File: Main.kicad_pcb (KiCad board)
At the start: 2 copper layers, 99.1 x 78.7 mm, 41 parts, among them J1 Conn_01x01_Female, J2 Conn_01x01_Female, J3 Conn_01x01_Female, J4 Conn_01x02_Female, J5 Conn_01x01_Female, J6 Conn_01x03, J7 Conn_01x03, Q1 CSD17307Q5A, Q2 CSD17307Q5A, Q3 Si6435ADQ, SW1 SW_Push, SW2 SW_Push, SW3 SW_Push, U1 LTC4002ES8-4.2, U3 LTC6995-1, U4 TPS2557

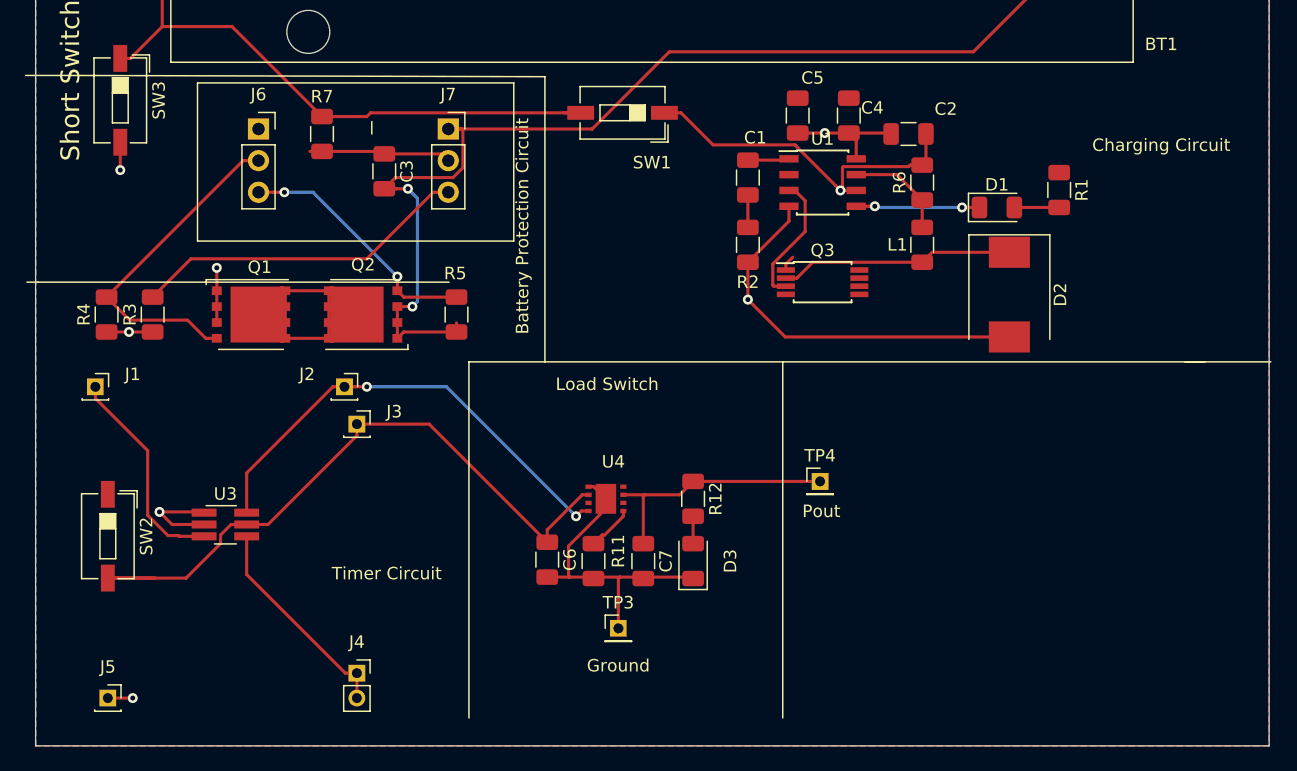
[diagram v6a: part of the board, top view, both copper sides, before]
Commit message: added final silk comments
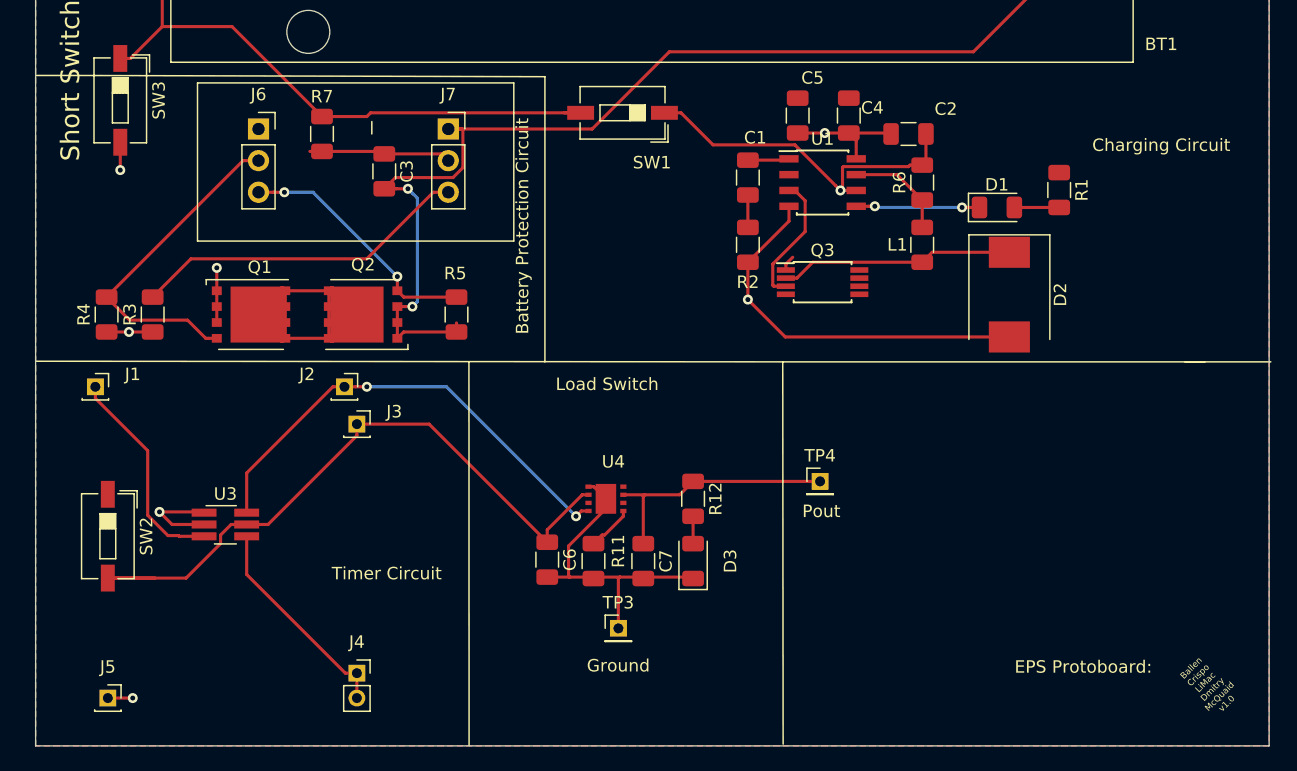
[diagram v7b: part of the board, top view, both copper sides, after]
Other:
- board text added: "Ballen Crispo LiMac Dmitry McQuaid v1.0"
- board text added: "EPS Protoboard:"
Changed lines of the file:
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@@
   (general
     (thickness 1.6)
-    (drawings 29)
+    (drawings 28)
     (tracks 229)
     (zones 0)
@@
     )
   )
+  (gr_text "EPS Protoboard:" (at 134.94 135.9) (layer F.SilkS)
+    (effects (font (size 1 1) (thickness 0.15)))
+  )
+  (gr_text "Ballen\nCrispo\nLiMac\nDmitry\nMcQuaid\nv1.0" (at 145.02 137.41 45) (layer F.SilkS)
+    (effects (font (size 0.5 0.5) (thickness 0.05)))
+  )
   (gr_line (start 50.8 142.24) (end 50.8 63.5) (layer Edge.Cuts) (width 0.05))
   (gr_line (start 149.86 142.24) (end 50.8 142.24) (layer Edge.Cuts) (width 0.05))
@@
     (effects (font (size 1.5 1.5) (thickness 0.3)))
   )
-  (gr_line (start 51 105) (end 50.1 105) (layer F.SilkS) (width 0.12))
-  (gr_line (start 52.6 88.4) (end 50 88.4) (layer F.SilkS) (width 0.12))
   (gr_line (start 143.1 111.4) (end 150 111.4) (layer F.SilkS) (width 0.12))
   (gr_text Pout (at 113.9 123.4) (layer F.SilkS)
@@
   )
   (gr_line (start 110.8 111.4) (end 144.7 111.4) (layer F.SilkS) (width 0.12))
-  (gr_line (start 53.7 88.4) (end 52.6 88.4) (layer F.SilkS) (width 0.12))
+  (gr_line (start 53.7 88.4) (end 50.82 88.4) (layer F.SilkS) (width 0.12))
   (gr_line (start 91.7 88.5) (end 53.7 88.4) (layer F.SilkS) (width 0.12))
   (gr_line (start 91.7 111.4) (end 91.7 88.5) (layer F.SilkS) (width 0.12))
@@
   (gr_line (start 89.2 101.7) (end 63.8 101.7) (layer F.SilkS) (width 0.12))
   (gr_line (start 89.2 89) (end 89.2 101.7) (layer F.SilkS) (width 0.12))
-  (gr_line (start 84 105) (end 51 105) (layer F.SilkS) (width 0.12))
   (gr_line (start 63.8 89) (end 89.2 89) (layer F.SilkS) (width 0.12))
-  (gr_line (start 110.8 111.4) (end 110.8 140) (layer F.SilkS) (width 0.12))
-  (gr_line (start 85.6 111.4) (end 110.8 111.4) (layer F.SilkS) (width 0.12))
+  (gr_line (start 110.8 111.4) (end 110.83 142.1) (layer F.SilkS) (width 0.12))
+  (gr_line (start 50.82 111.35) (end 110.8 111.4) (layer F.SilkS) (width 0.12))
   (gr_text "Charging Circuit" (at 141.2 94) (layer F.SilkS)
     (effects (font (size 1 1) (thickness 0.15)))
@@
   )
   (gr_line (start 77.8 92.1) (end 77.8 93.1) (layer F.SilkS) (width 0.12))
-  (gr_line (start 85.6 111.4) (end 85.6 140) (layer F.SilkS) (width 0.12))
+  (gr_line (start 85.6 111.4) (end 85.61 142.22) (layer F.SilkS) (width 0.12))
   (segment (start 54.9 70.925) (end 54.9 70) (width 0.25) (layer F.Cu) (net 1))
   (segment (start 54.9 74.75) (end 54.9 70.925) (width 0.25) (layer F.Cu) (net 1))

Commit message: added changes mark wante
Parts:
- removed D3: LED, LED_SMD:LED_1206_3216Metric
- removed L1: 1.64u, Inductor_SMD:L_1206_3216Metric
- removed R11: 20k, Resistor_SMD:R_1206_3216Metric
- removed R12: 2k, Resistor_SMD:R_1206_3216Metric
- added J10: Conn_01x01_Female, Connector_PinSocket_2.00mm:PinSocket_1x01_P2.00mm_Vertical, F.Cu at (102.8, 133.9)
- added J11: Conn_01x01_Female, Connector_PinSocket_2.00mm:PinSocket_1x01_P2.00mm_Vertical, F.Cu at (148.0, 100.8)
- added J12: Conn_01x01_Female, Connector_PinSocket_2.00mm:PinSocket_1x01_P2.00mm_Vertical, F.Cu at (122.0, 100.8)
- added J8: Conn_01x06, Connector_PinHeader_2.00mm:PinHeader_1x06_P2.00mm_Vertical, F.Cu at (95.2, 98.3)
- added J9: Conn_01x01_Female, Connector_PinSocket_2.00mm:PinSocket_1x01_P2.00mm_Vertical, F.Cu at (102.8, 113.2)
- added SW4: SW_Push, Button_Switch_SMD:SW_DIP_SPSTx01_Slide_6.7x4.1mm_W6.73mm_P2.54mm_LowProfile_JPin, F.Cu at (99.8, 99.5)
- added TP5: TestPoint, Connector_PinHeader_2.00mm:PinHeader_1x01_P2.00mm_Vertical, F.Cu at (129.4, 90.8)
- added TP6: TestPoint, Connector_PinHeader_2.00mm:PinHeader_1x01_P2.00mm_Vertical, F.Cu at (132.6, 90.8)
- moved TP3 7.28 mm to (91.6, 136.9)
- moved C6 5.21 mm to (91.6, 132.5)
- moved TP4 5.21 mm to (113.5, 126.2)
- moved U4 5.21 mm to (95.0, 126.6)
- moved C7 5.21 mm to (99.3, 132.6)
- moved Q3 0.95 mm to (114.8, 105.5)
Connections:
- net Net-(BT1-Pad2) renamed /BQ29707_P4
- net Net-(C3-Pad1) renamed /BQ29707_P5
- net Net-(J6-Pad2) renamed /BQ29707_P2
- net Net-(J6-Pad3) renamed /BQ29707_P3
- net Net-(J7-Pad3) renamed /BQ29707_P6
- J6 pad 1: Net-(J6-Pad1) -> /BQ29707_P1
- U1 pad 1: Net-(C1-Pad1) -> Net-(SW4-Pad2)
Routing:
- net /BQ29707_P1: track 0.00 -> 29.8 mm
- net /BQ29707_P2: track 27.0 -> 56.5 mm
- net Net-(D2-Pad1): track 18.8 -> 38.9 mm
- net Net-(SW4-Pad2): track 0.00 -> 16.0 mm
- net Net-(J12-Pad1): track 8.34 -> 24.3 mm
- net /BQ29707_P5: track 11.4 -> 27.2 mm
- net /BQ29707_P6: track 27.2 -> 42.8 mm
- net Net-(J9-Pad1): track 3.74 -> 19.2 mm, vias 0 -> 1
- net /BQ29707_P4: track 105.2 -> 117.7 mm
- net /BQ29707_P3: track 20.1 -> 32.2 mm
- net Net-(C2-Pad1): track 30.5 -> 39.1 mm
- net GNDD: track 86.3 -> 78.7 mm
- net Net-(C1-Pad1): track 3.82 -> 9.06 mm
- net Net-(J2-Pad1): track 38.0 -> 43.1 mm
- net Net-(C6-Pad1): track 54.6 -> 58.2 mm
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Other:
- board text added: "BQ29707 Pin1"
- board text added: "Bat to Charger"
- board text added: "Comp Pin"
- board text added: "Timer Power"
